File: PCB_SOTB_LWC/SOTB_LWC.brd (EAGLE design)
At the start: 123.2 x 118.1 mm, 99 parts, among them IC1 LP38511MR-ADJ_NOPB, IC2 LP38511MR-ADJ_NOPB, IC3 LP38511MR-ADJ_NOPB, IC4 SN74LVC1GU04DCKR, IC5 SN74LVC1G14DCKR, J1 2985-6004, Y2 Q13FC1350000400

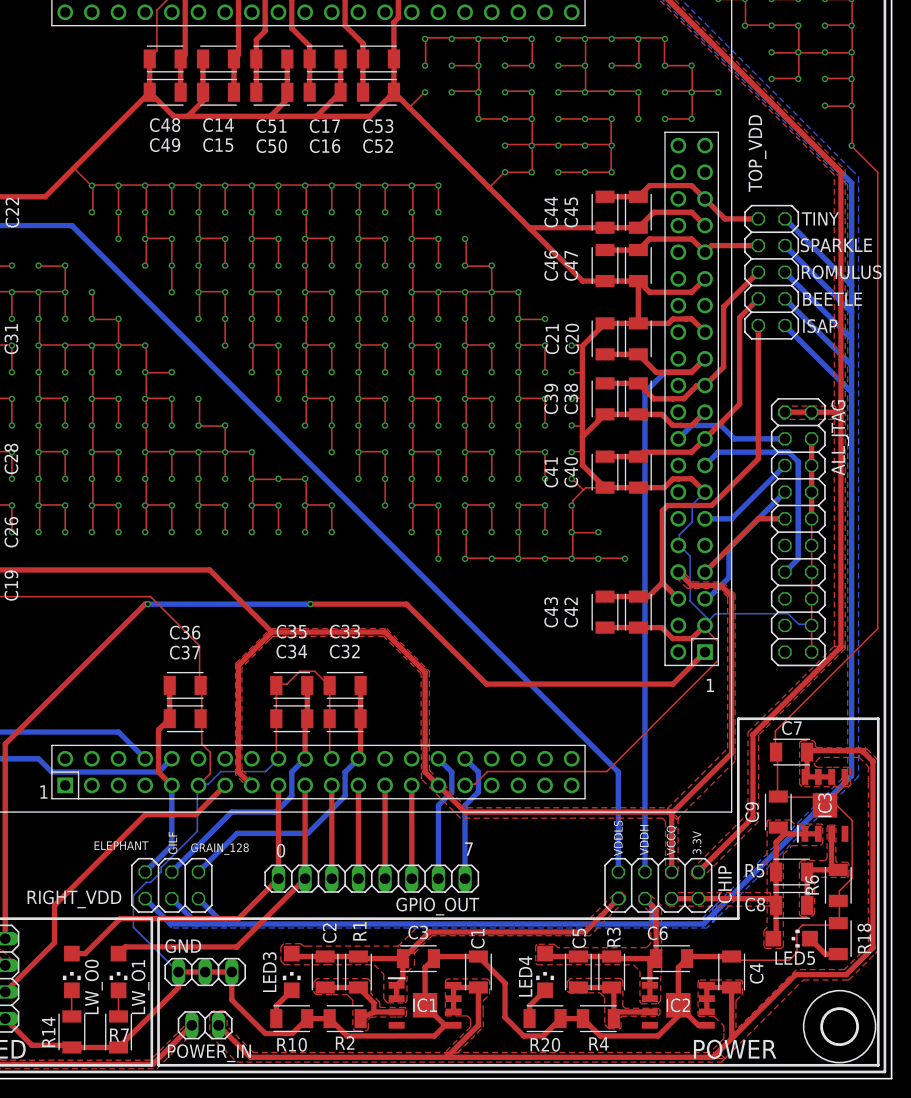
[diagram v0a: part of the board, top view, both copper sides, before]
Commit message: Change led from 1206 to 0805
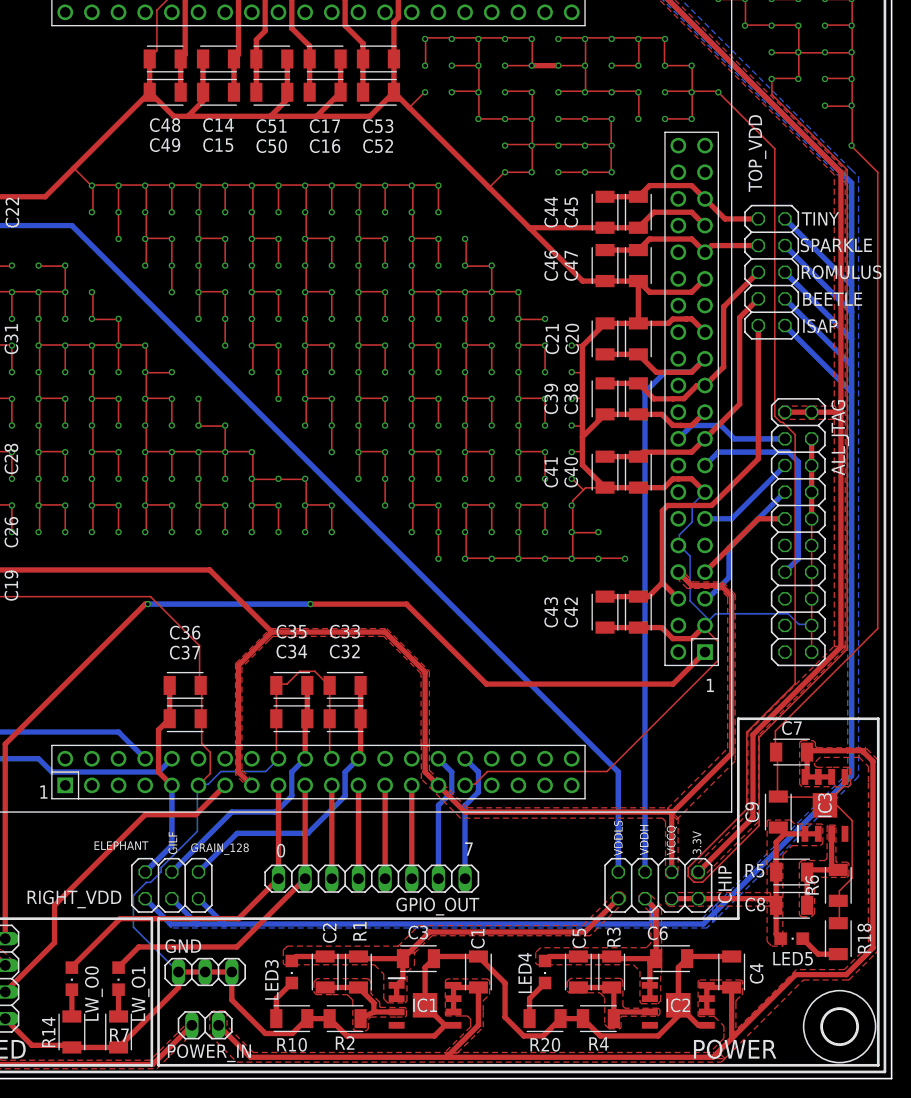
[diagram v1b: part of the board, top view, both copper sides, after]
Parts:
- LED3, LED4, LED5, LW_O0, LW_O1: device led:CHIPLED_1206 -> led:CHIPLED_0805
- moved LW_O0 0.63 mm to (-19.7, -56.5)
- moved LW_O1 0.63 mm to (-15.2, -56.5)
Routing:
- net GND: track 1987.8 -> 2146.1 mm
- net N$9: track 3.31 -> 4.01 mm
- net N$10: track 3.31 -> 4.01 mm
- net N$11: track 3.31 -> 4.01 mm
- net RS_LW_SOC_O0: track 31.5 -> 32.1 mm
- net RS_LW_SOC_O1: track 29.6 -> 30.2 mm
